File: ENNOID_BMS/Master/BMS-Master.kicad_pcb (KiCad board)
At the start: 2 copper layers, 135 x 130 mm, 245 parts, among them J1 Contactor+, J10 Charge, J11 CAN, J13 Charger, J14 SERIAL, J15 Charge +, J16 ISOSPI_TEMP, J17 DEBUG, J18 OLED, J19 ISOSPI_CELL, J2 Cooling, J20 USB_C_Receptacle_USB2.0_16P, J21 INV_Power, J3 + 12V -, J4 Contactor-, J5 BAT_Power, J6 Power Button, J7 E-Stop, J8 Discharge, J9 Discharge, K1 SHV12-1A85-78L3K, Q1 BSS138, Q2 BSS138, Q26 BSS138, Q27 BSS138, Q28 BSS138, Q29 BSS138, Q3 BSS138, Q30 BSS138, Q4 BUK98150-55A, Q5 BUK98150-55A, Q6 BUK98150-55A, Q7 BUK98150-55A, Q8 BUK98150-55A, Q9 BSS138, U1 AMC1301 or AMC1302, U10 SN6501DBV, U11 LTC6820, U12 AMC1301, U13 AMC1301, U14 OPA2197IDR, U16 ISL28022, U17 STM32F303CCTx, U19 LM5165YDRC, U2 LTC6820, U3 TPS76350, U4 SN6501DBV, U5 SFH617A-2X009T, U6 TPS76350, U7 CP2104, U8 ISO1050DUBR, U9 SFH617A-2X009T, Y1 8MHz

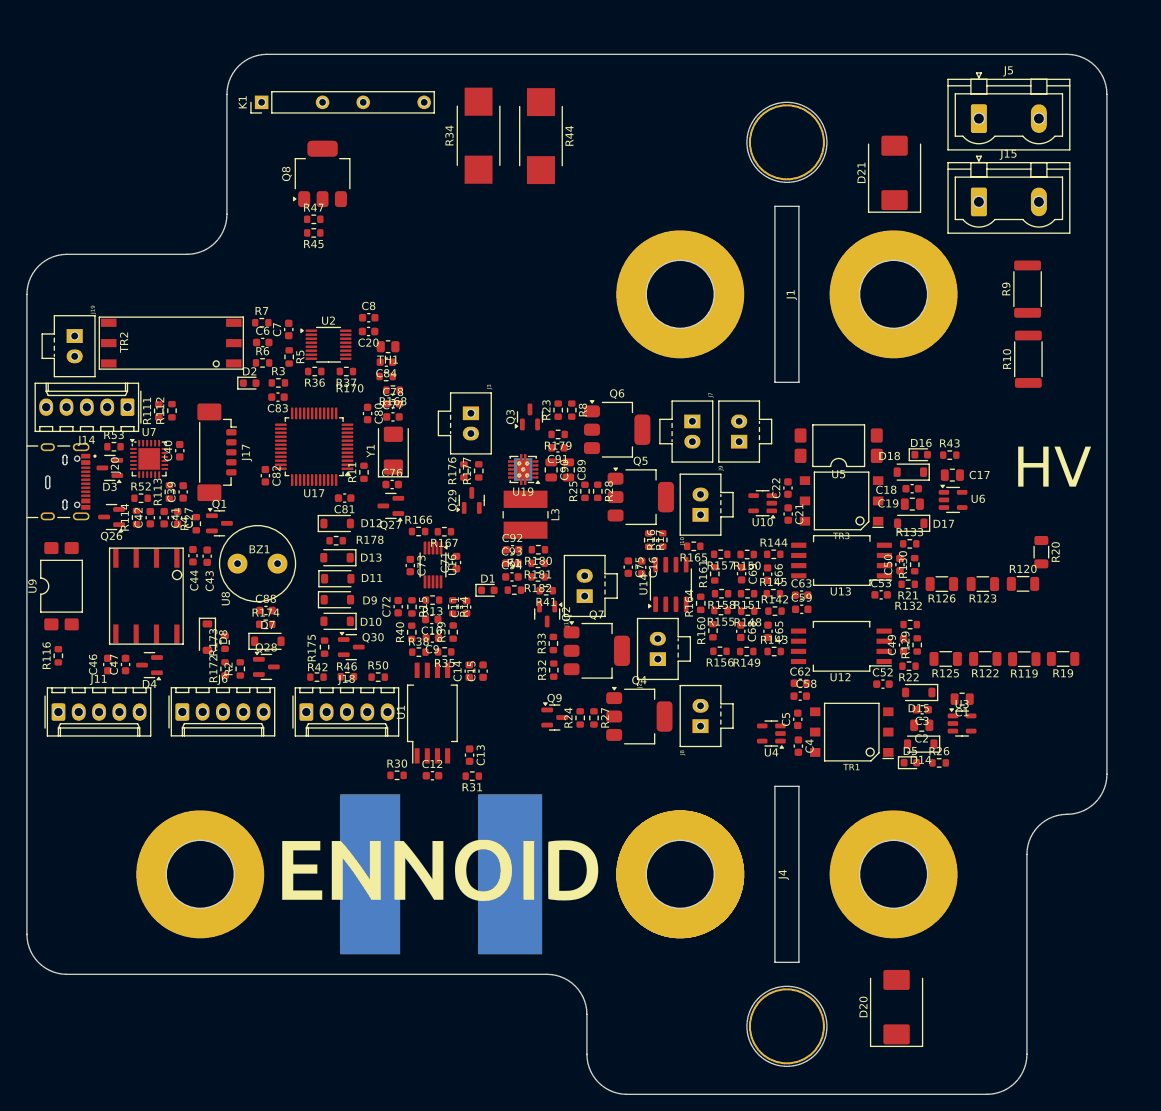
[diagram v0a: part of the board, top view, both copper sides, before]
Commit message: slave with new fuses added
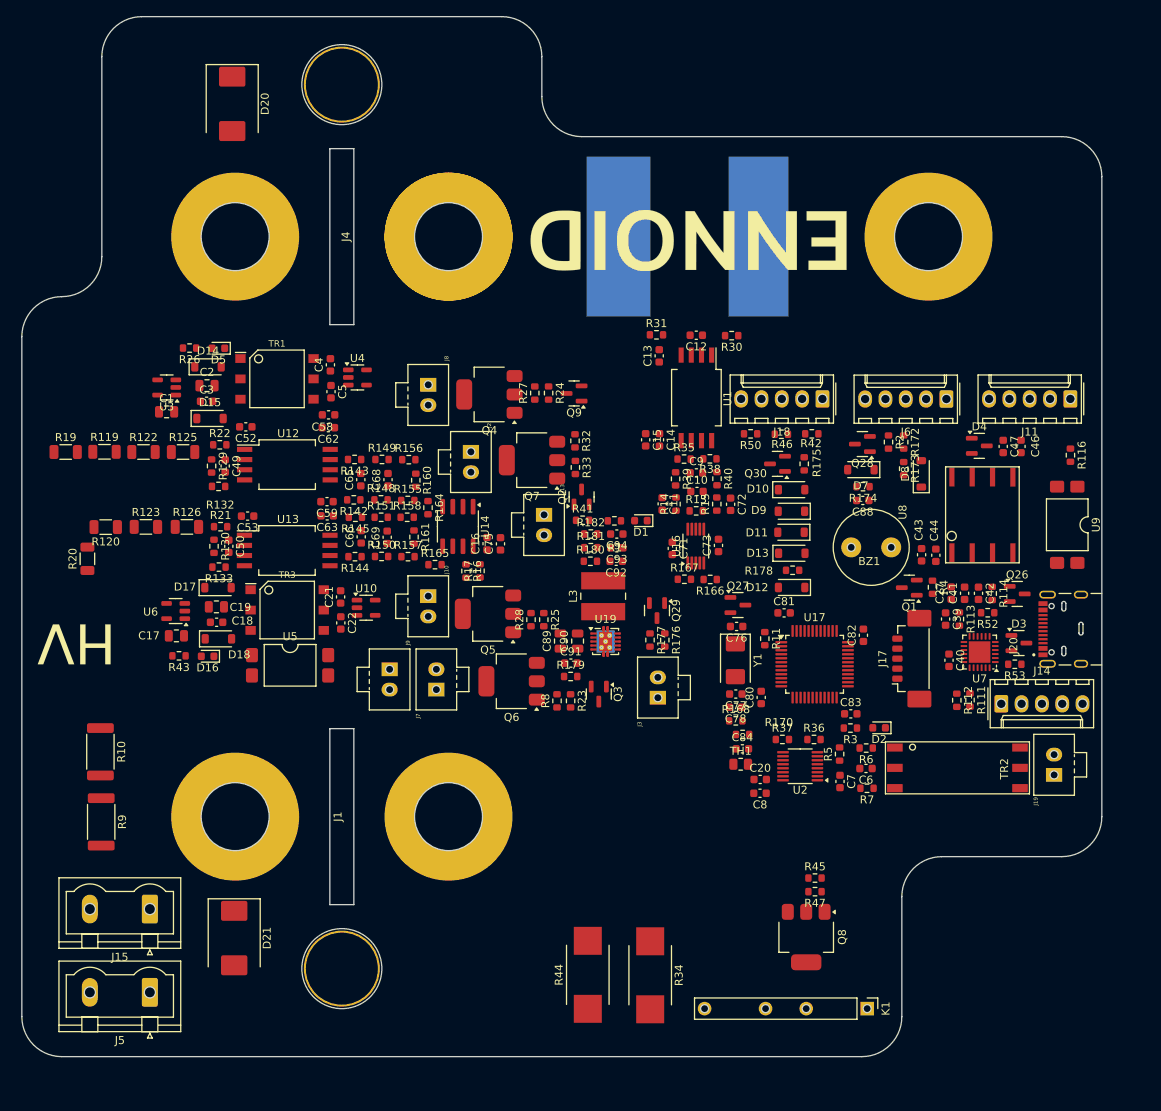
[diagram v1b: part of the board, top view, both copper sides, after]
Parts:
- moved J5 150.6 mm to (54.2, 151.6), turned to 180 degrees
- moved D20 140.2 mm to (64.5, 40.5), turned to -90 degrees
- moved K1 136.2 mm to (143.8, 153.6), turned to -90 degrees
- moved J15 136.2 mm to (54.2, 141.1), turned to 180 degrees
- moved J20 135.6 mm to (173.2, 106.2), turned to 90 degrees
- moved J19 134.2 mm to (167.2, 124.4), turned to 180 degrees
- moved R9 133.6 mm to (48.1, 130.2), turned to -90 degrees
- moved J11 132.4 mm to (169.2, 77.4), turned to 180 degrees
- moved R116 129.0 mm to (169.3, 84.4), turned to -90 degrees
- moved R19 127.3 mm to (43.7, 84.0), turned to 0 degrees
- moved D21 126.3 mm to (64.7, 144.8), turned to -90 degrees
- moved U9 125.9 mm to (168.9, 93.1), turned to -90 degrees
- moved R10 125.9 mm to (48.0, 121.5), turned to -90 degrees
- moved R20 119.2 mm to (46.4, 97.4), turned to 90 degrees
- moved R119 117.9 mm to (48.5, 84.0), turned to 0 degrees
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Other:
- outline, holes or cut-outs redrawn

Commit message: Slave with SMD and no other fuses
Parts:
- removed BZ1: AI-1027-TWT-5V, ENNOID:BUZZER
- removed C84: 100n, Capacitor_SMD:C_0603_1608Metric
- removed J18: OLED, Connector_Molex:Molex_KK-254_AE-6410-05A_1x05_P2.54mm_Vertical
- removed the J2 at (94.3, 84.0)
- removed J20: USB_C_Receptacle_USB2.0_16P, ENNOID:SAMESKY_UJ20-C-H-G-SMT-1-P16-TR
- removed the J7 at (90.0, 113.7)
- removed the J8 at (89.0, 75.6)
- removed K1: SHV12-1A85-78L3K, ENNOID:SHV12-1AB5-7BL3K
- removed LOGO1: Logo_Open_Hardware_Small, ENNOID:ENNOID-LOGO
- removed the Q1 at (149.1, 101.0)
- removed the Q3 at (110.3, 114.3)
- removed the Q4 at (96.6, 76.8)
- removed the Q5 at (96.5, 104.2)
- removed the Q6 at (99.4, 112.7)
- removed the R11 at (131.1, 107.3)
- removed R170: 100k, Resistor_SMD:R_0603_1608Metric
- removed the R23 at (106.8, 115.1)
- removed the R24 at (104.0, 76.6)
- removed the R25 at (103.4, 105.0)
- removed the R27 at (102.3, 76.6)
- removed the R28 at (101.8, 105.0)
- removed the R32 at (107.3, 82.6)
- removed the R33 at (107.4, 85.9)
- removed the R34 at (116.7, 149.4)
- removed the R4 at (152.0, 100.9)
- removed the R42 at (136.9, 81.7)
- removed the R44 at (108.9, 149.4)
- removed the R45 at (137.3, 137.3)
- removed the R46 at (133.1, 81.8)
- removed the R47 at (137.3, 139.0)
- removed the R50 at (129.3, 81.7)
- removed the R8 at (105.1, 115.1)
- removed TH1: Thermistor_NTC 100K, Resistor_SMD:R_0805_2012Metric
- added G***: LOGO, LOGO, F.Cu at (49.8, 79.0)
- added G***: LOGO, LOGO, F.Cu at (120.6, 56.4)
- added J17: UJ20-C-H-G-SMT-1-P16-TR, Kicad_Libraries:SAMESKY_UJ20-C-H-G-SMT-1-P16-TR, F.Cu at (173.1, 116.0)
- added Q10: BSS138, Package_TO_SOT_SMD:SOT-23, F.Cu at (149.1, 120.0)
- added R81: 10, Resistor_SMD:R_0603_1608Metric, F.Cu at (136.9, 116.5)
- added R82: 10, Resistor_SMD:R_0603_1608Metric, F.Cu at (139.1, 120.0)
- added R83: 10, Resistor_SMD:R_0603_1608Metric, F.Cu at (146.0, 116.3)
- added R84: 10, Resistor_SMD:R_0603_1608Metric, F.Cu at (146.2, 120.0)
- J1: renamed from J5; footprint Connector_Phoenix_GMSTB:PhoenixContact_GMSTBVA_2,5_2-G_1x02_P7.50mm_Vertical -> Kicad_Libraries:Phoenix_1x2_1729128
- J10: value Charge -> LVE_Shutdown; footprint ENNOID:Pin_1x02-XL -> Connector_JST:JST_XH_B2B-XH-A_1x02_P2.50mm_Vertical
- J11: footprint Connector_Molex:Molex_KK-254_AE-6410-05A_1x05_P2.54mm_Vertical -> Connector_JST:JST_XH_B5B-XH-A_1x05_P2.50mm_Vertical
- J13: renamed from J15; footprint Connector_Phoenix_GMSTB:PhoenixContact_GMSTBVA_2,5_2-G_1x02_P7.50mm_Vertical -> Kicad_Libraries:Phoenix_1x2_1729128
- J14: renamed from J13; footprint ENNOID:Pin_1x02-XL -> Connector_JST:JST_XH_B2B-XH-A_1x02_P2.50mm_Vertical
- J15: renamed from J17; footprint Connector_Molex:Molex_PicoBlade_53398-0571_1x05-1MP_P1.25mm_Vertical -> Connector_JST:JST_XH_B5B-XH-A_1x05_P2.50mm_Vertical
- J16: renamed from J14; footprint Connector_Molex:Molex_KK-254_AE-6410-05A_1x05_P2.54mm_Vertical -> Connector_JST:JST_XH_B5B-XH-A_1x05_P2.50mm_Vertical
- J4: renamed from J3; footprint ENNOID:Pin_1x02-XL -> Connector_JST:JST_XH_B2B-XH-A_1x02_P2.50mm_Vertical
- J5: renamed from J6; footprint Connector_Molex:Molex_KK-254_AE-6410-05A_1x05_P2.54mm_Vertical -> Connector_JST:JST_XH_B5B-XH-A_1x05_P2.50mm_Vertical
- J6: renamed from J21; footprint Connector_Phoenix_GMSTB:PhoenixContact_GMSTBVA_2,5_2-G_1x02_P7.50mm_Vertical -> Kicad_Libraries:Phoenix_1x2_1729128
- J7: renamed from J19; footprint ENNOID:Pin_1x02-XL -> Connector_JST:JST_XH_B2B-XH-A_1x02_P2.50mm_Vertical
- J8: renamed from J16; footprint ENNOID:Pin_1x02-XL -> Connector_JST:JST_XH_B2B-XH-A_1x02_P2.50mm_Vertical
- J9: value Discharge -> Charger_Shutdown; footprint ENNOID:Pin_1x02-XL -> Connector_JST:JST_XH_B2B-XH-A_1x02_P2.50mm_Vertical
- Q7, Q8: value BUK98150-55A -> BSS138; footprint Package_TO_SOT_SMD:SOT-223 -> Package_TO_SOT_SMD:SOT-23
- U6: renamed from U1; value AMC1301 or AMC1302 -> AMC1302
- moved J6 226.5 mm to (91.7, 167.8)
- moved J8 191.2 mm to (118.8, 147.7)
- moved TR4 148.3 mm to (120.1, 135.0), turned to 180 degrees
- moved R72 133.3 mm to (117.4, 123.8), turned to 90 degrees
- moved R68 132.1 mm to (118.4, 121.3), turned to 180 degrees
- moved R76 131.2 mm to (123.3, 114.7), turned to -90 degrees
- moved R74 131.1 mm to (123.4, 118.0), turned to 90 degrees
- moved C50 128.0 mm to (115.0, 118.3), turned to -90 degrees
- moved R71 127.9 mm to (122.5, 123.8), turned to -90 degrees
- moved U14 127.0 mm to (120.1, 116.3), turned to -90 degrees
- moved C52 126.4 mm to (116.8, 118.3), turned to 90 degrees
- moved C46 122.4 mm to (120.0, 123.8), turned to 90 degrees
- moved C48 120.9 mm to (121.7, 121.4)
- moved J10 63.5 mm to (148.2, 124.9)
- moved Q9 57.4 mm to (148.9, 116.2), turned to 0 degrees
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- renumbered C53 to C10, C50 to C11, C13 to C12, C14 to C13, C58 to C14, C59 to C15, C4 to C16, C21 to C17, C15 to C18, C62 to C19, C17 to C2, C63 to C20, C5 to C21, C9 to C23, C65 to C24, C66 to C25, C10 to C26, C68 to C27, C69 to C28, C71 to C29, C11 to C30, C73 to C31, C72 to C32, C16 to C33, C75 to C34, C88 to C35, C89 to C36, C90 to C37, C91 to C38, C92 to C39, C18 to C4, C93 to C40, C94 to C41, C76 to C42, C77 to C43, C78 to C44, C6 to C45, C23 to C46, C7 to C47, C24 to C48, C20 to C49, C2 to C5, C25 to C50, C8 to C51, C26 to C52, C80 to C53, C81 to C54, C82 to C55, C83 to C56, C39 to C57, C27 to C58, C40 to C59, C19 to C6, C41 to C60, C42 to C61, C43 to C62, C44 to C63, C46 to C64, C47 to C65, C12 to C7, C52 to C8, C49 to C9, D21 to D1, D18 to D10, D7 to D11, D8 to D12, D9 to D13, D10 to D14, D11 to D15, D12 to D16, D13 to D17, D3 to D18, D4 to D19, D20 to D2, D1 to D3, D2 to D4, D16 to D6, D14 to D7, D15 to D8, D17 to D9, J1 to J2, J4 to J3, L3 to L1, Q2 to Q1, Q28 to Q2, Q29 to Q3, Q30 to Q4, Q27 to Q5, Q26 to Q6, R2 to R1, R9 to R10, R119 to R11, R120 to R12, R122 to R13, R123 to R14, R10 to R15, R29 to R16, R125 to R17, R126 to R18, R129 to R19, R1 to R2, R130 to R20, R30 to R21, R31 to R22, R132 to R23, R21 to R24, R133 to R25, R22 to R26, R35 to R27, R38 to R28, R142 to R29, R143 to R30, R144 to R31, R145 to R32, R39 to R33, R40 to R34, R148 to R35, R149 to R36, R150 to R37, R151 to R38, R155 to R39, R52 to R4, R156 to R40, R157 to R41, R158 to R42, R14 to R43, R15 to R44, R160 to R45, R161 to R46, R13 to R47, R164 to R48, R165 to R49, R53 to R5, R166 to R50, R16 to R51, R17 to R52, R167 to R53, R41 to R54, R172 to R55, R173 to R56, R174 to R57, R175 to R58, R176 to R59, R26 to R6, R177 to R60, R178 to R61, R179 to R62, R180 to R63, R181 to R64, R182 to R65, R168 to R66, R5 to R67, R12 to R68, R6 to R69, R43 to R7, R7 to R70, R18 to R71, R48 to R72, R36 to R73, R49 to R74, R37 to R75, R51 to R76, R111 to R77, R112 to R78, R113 to R79, R19 to R8, R114 to R80, R116 to R85, R20 to R9, TR3 to TR2, TR2 to TR3, U3 to U1, U16 to U10, U19 to U11, U17 to U12, U2 to U13, U11 to U14, U7 to U15, U8 to U16, U9 to U17, U6 to U2, U12 to U3, U13 to U4, U4 to U7, U10 to U8, U14 to U9
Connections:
- C31 pad 2: +3.3V -> +3V3
- C49 pad 2: +3.3V -> +3V3
- C50 pad 2: +3.3V -> +3V3
- C51 pad 1: +3.3V -> +3V3
- C52 pad 1: +3.3V -> +3V3
- J10 pad 1: +12V -> /BMS_OK/Multipurpose_enable_S
- J10 pad 2: /switches/Charge -> /BMS_OK/Discharge_enable_S
- J13 pad 1: /Load+ -> Net-(J13-Pin_1)
- J13 pad 2: Net-(J15-Pin_2) -> /Load+
- J9 pad 1: +12V -> /BMS_OK/Charger_Safety_S
- J9 pad 2: Net-(J7-Pin_1) -> /BMS_OK/Charge_enable_S
- Q7 pad 2: /switches/Cooling -> GND
- Q7 pad 3: GND -> /BMS_OK/Charge_enable_S
- Q8 pad 2: /switches/Precharge -> GND
- Q8 pad 3: GND -> /BMS_OK/Charger_Safety_S
- Q9 pad 1: /MCU/Safety -> Net-(Q9-G)
- Q9 pad 3: /MCU/DischargeNegEnable -> /BMS_OK/Discharge_enable_S
- R10 pad 2: Net-(J15-Pin_2) -> Net-(J13-Pin_1)
- R50 pad 1: +3.3V -> +3V3
- R53 pad 1: +3.3V -> +3V3
- R75 pad 1: +3.3V -> +3V3
- R76 pad 1: +3.3V -> +3V3
- U10 pad 6: +3.3V -> +3V3
- U12 pad 10: /MCU/NTC_Switch -> unconnected-(U12-ADC1_IN1/COMP1_INM/COMP1_OUT/COMP7_INP/RTC_TAMP2/SYS_WKUP1/TIM2_CH1/TIM2_ETR/TIM8_BKIN/TIM8_ETR/TSC_G1_IO1/USART2_CTS/PA0-Pad10)
- U12 pad 18: /MCU/ChargeEnable -> /BMS_OK/Charge_enable
- U12 pad 2: /MCU/Safety -> unconnected-(U12-PC13/RTC_OUT_ALARM/RTC_OUT_CALIB/RTC_TAMP1/RTC_TS/SYS_WKUP2/TIM1_CH1N-Pad2)
- U12 pad 20: /MCU/CoolingEnable -> /BMS_OK/Charger_Safey
- U12 pad 21: /MCU/DischargePosEnable -> /BMS_OK/Discharge_enable
- U12 pad 22: /MCU/PreChargeEnable -> /BMS_OK/Multipurpose_enable
- U12 pad 38: /MCU/BUZZER -> unconnected-(U12-ADC1_EXTI15/ADC2_EXTI15/I2C1_SCL/I2S3_WS/SPI1_NSS/SPI3_NSS/SYS_JTDI/TIM1_BKIN/TIM2_CH1/TIM2_ETR/TIM8_CH1/USART2_RX/PA15-Pad38)
- U12 pad 4: /MCU/DischargeNegEnable -> unconnected-(U12-PC15/ADC1_EXTI15/ADC2_EXTI15/RCC_OSC32_OUT-Pad4)
- U12 pad 42: /MCU/OLED_SCL -> unconnected-(U12-PB6/I2C1_SCL/TIM16_CH1N/TIM4_CH1/TIM8_BKIN2/TIM8_CH1/TIM8_ETR/TSC_G5_IO3/USART1_TX-Pad42)
- U12 pad 43: /MCU/OLED_SDA -> unconnected-(U12-PB7/I2C1_SDA/TIM17_CH1N/TIM3_CH4/TIM4_CH2/TIM8_BKIN/TSC_G5_IO4/USART1_RX-Pad43)
- U12 pad 45: /MCU/OLED_RST -> unconnected-(U12-PB8/CAN_RX/COMP1_OUT/I2C1_SCL/TIM16_CH1/TIM1_BKIN/TIM4_CH3/TIM8_CH2/TSC_SYNC-Pad45)
- U13 pad 1: +3.3V -> +3V3
- U13 pad 12: +3.3V -> +3V3
- U13 pad 6: +3.3V -> +3V3
- U13 pad 7: +3.3V -> +3V3
- U13 pad 8: +3.3V -> +3V3
- U13 pad 9: +3.3V -> +3V3
- U14 pad 1: +3.3V -> +3V3
- U14 pad 12: +3.3V -> +3V3
- U14 pad 6: +3.3V -> +3V3
- U14 pad 7: +3.3V -> +3V3
- U14 pad 8: +3.3V -> +3V3
- U14 pad 9: +3.3V -> +3V3
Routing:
- net +3V3: track 0.00 -> 356.3 mm, vias 0 -> 23
- net GNDA: track 0.00 -> 232.8 mm, vias 0 -> 7
- net GNDREF: track 0.00 -> 189.4 mm, vias 0 -> 1
- net GND: track 0.00 -> 147.3 mm, vias 0 -> 13
- net /Load+: track 0.00 -> 144.8 mm
- net /BAT+: track 0.00 -> 100.2 mm, vias 0 -> 1
- net /PowerMonitor/ISO+5V: track 0.00 -> 89.6 mm
- net /PowerSupply/ChargeDetect: track 0.00 -> 83.3 mm, vias 0 -> 3
- net /PowerMonitor/Current: track 0.00 -> 79.5 mm, vias 0 -> 1
- net +12V: track 0.00 -> 74.4 mm, vias 0 -> 4
- net /MCU/MOSI: track 0.00 -> 47.4 mm, vias 0 -> 2
- net /CAN/EnableRequest: track 0.00 -> 45.9 mm, vias 0 -> 2
- net /MCU/SCK: track 0.00 -> 44.0 mm, vias 0 -> 2
- net /MCU/MISO: track 0.00 -> 44.0 mm, vias 0 -> 2
- net /MCU/TX_USB: track 0.00 -> 43.2 mm, vias 0 -> 2
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- added copper zone on F.Cu, net GND
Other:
- board size 135 x 130 mm -> 135 x 145 mm
- board text added: "LV"

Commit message: master and slave updated
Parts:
- moved D1 14.4 mm to (64.4, 178.6)
- moved J1 14.4 mm to (45.0, 164.8)
- moved J13 14.4 mm to (45.1, 177.1)
- moved J2 14.4 mm to (78.1, 159.5)
- moved J6 14.4 mm to (91.6, 182.2)
- moved R10 14.4 mm to (48.0, 153.1)
- moved R15 14.4 mm to (47.9, 144.3)
- moved C5 11.8 mm to (67.7, 91.6)
- moved D5 11.8 mm to (59.3, 94.5)
- moved D7 11.8 mm to (68.2, 89.3)
- moved D8 11.8 mm to (66.8, 95.7)
- moved R6 11.8 mm to (59.3, 91.0)
- moved C3 11.8 mm to (67.7, 93.5)
- moved C1 11.8 mm to (62.6, 92.9)
- moved U1 11.8 mm to (62.6, 89.9)
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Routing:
- net GNDREF: track 189.4 -> 209.6 mm
- net GNDA: track 232.8 -> 251.1 mm
- net /PowerSupply/ChargeDetect: track 83.3 -> 96.4 mm
- net /PowerMonitor/ISO+5V: track 89.6 -> 101.7 mm
- net Net-(U9B--): track 7.43 -> 17.6 mm
- net Net-(U9B-+): track 6.33 -> 14.7 mm, vias 2 -> 0
- net Net-(U9A--): track 9.89 -> 17.5 mm
- net Net-(U9A-+): track 11.1 -> 16.8 mm
- net /MCU/CS_CELL: track 26.2 -> 20.9 mm
- net /MCU/SCK: track 44.0 -> 39.1 mm
- net /MCU/MOSI: track 47.4 -> 43.0 mm
- net +3V3: track 356.3 -> 351.9 mm, vias 23 -> 21
- net +12V: track 74.4 -> 77.7 mm
- net Net-(R15-Pad1): track 31.6 -> 34.1 mm
- net /Load+: track 144.8 -> 147.3 mm
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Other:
- board size 135 x 145 mm -> 135.1 x 159.4 mm
- board text added: "12V+"
- board text added: "3V3+"
- board text added: "5V"
- board text added: "A+"
- board text added: "A-"
- board text added: "Aux+"
- board text added: "Aux-"
- board text added: "BAT+"
- board text added: "BAT-"
- board text added: "Button"
- board text added: "CAN"
- board text added: "Cell"
- board text added: "Charger"
- board text added: "EN"
- board text added: "GND"
- board text added: "H"
- board text added: "L"
- board text added: "LED"
- board text added: "Load+"
- board text added: "Load-"
- board text added: "NRST"
- board text added: "SWCLK"
- board text added: "SWDIO"
- board text added: "Temp"

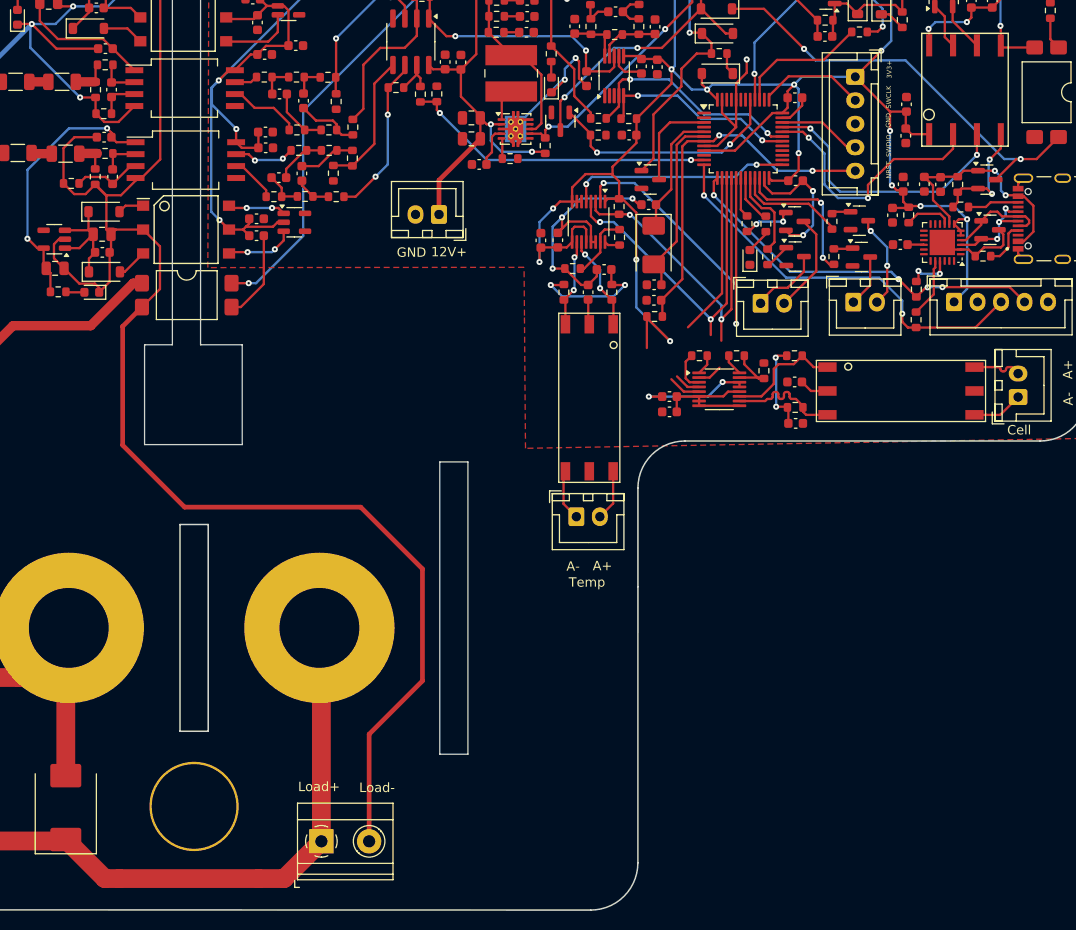
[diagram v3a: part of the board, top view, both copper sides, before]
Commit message: new cells and updated slave
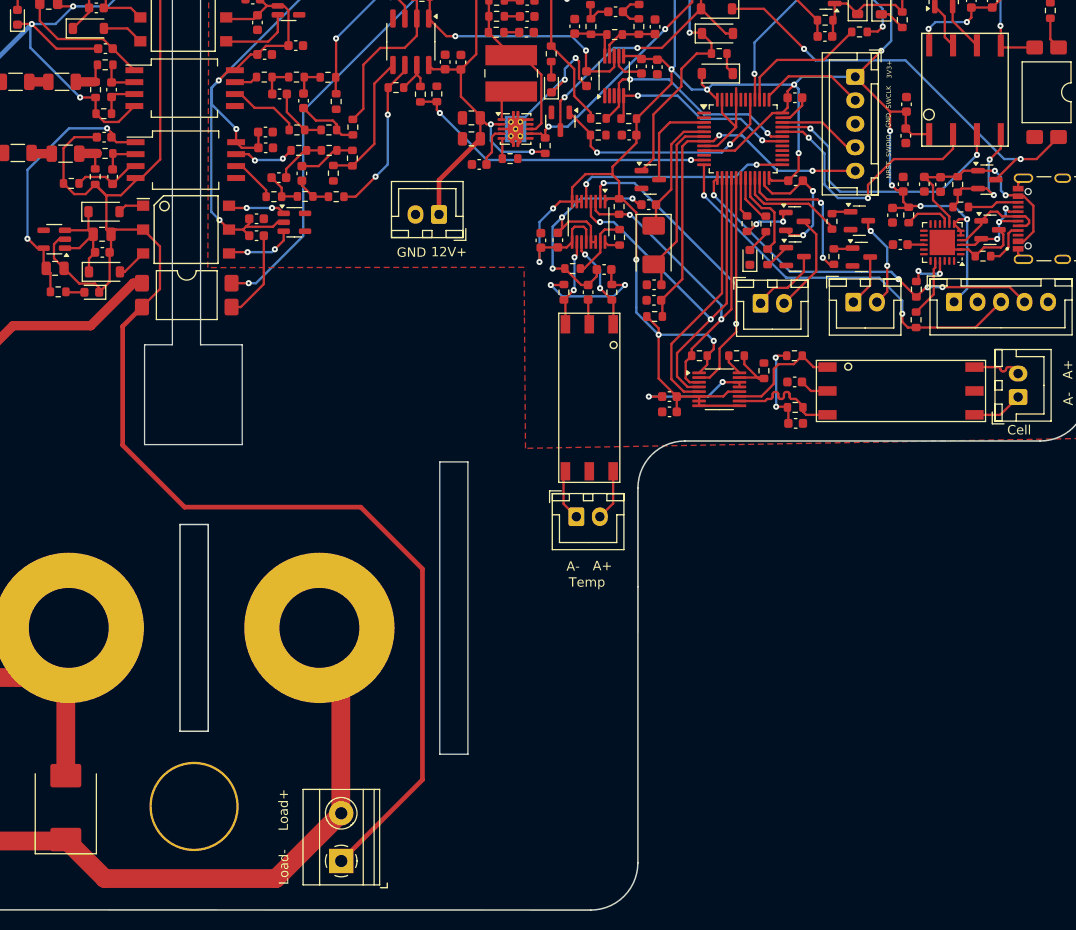
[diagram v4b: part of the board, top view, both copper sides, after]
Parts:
- moved J6 2.97 mm to (93.7, 184.3), turned to 90 degrees
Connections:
- J6 pad 1: /Load+ -> GNDREF
- J6 pad 2: GNDREF -> /Load+
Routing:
- net +3V3: track 351.9 -> 361.5 mm, vias 21 -> 22
- net /MCU/CS_CELL: track 20.9 -> 27.1 mm
- net /MCU/SCK: track 39.1 -> 45.0 mm
- net /Load+: track 147.3 -> 152.8 mm
- net /MCU/MOSI: track 43.0 -> 48.4 mm
- net GNDREF: track 209.6 -> 212.9 mm
- net GND: track 147.3 -> 144.3 mm, vias 13 -> 12
- net /MCU/MISO: track 42.0 -> 44.9 mm
